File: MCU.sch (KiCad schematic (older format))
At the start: 9 parts

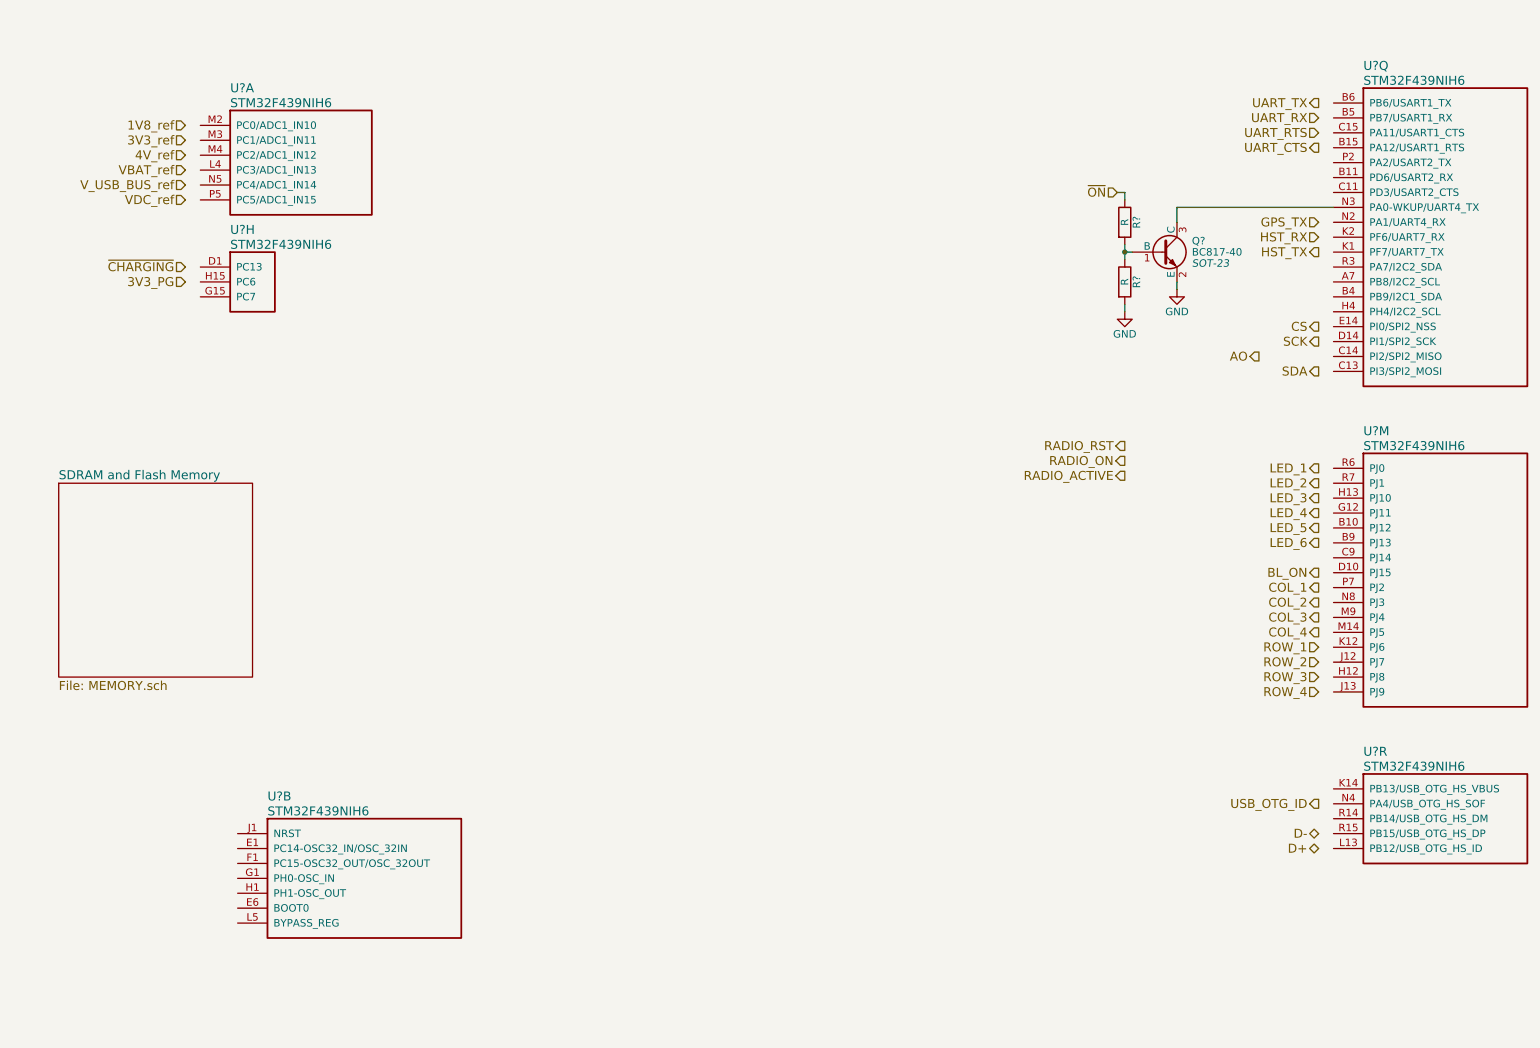
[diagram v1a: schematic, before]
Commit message: current version of the schematics. Audio circuits are still missing.
Audio curcuit topology
Audio from cellphone module is routed to STM
Audio from microphone is routed to STM
STM processes audio and routes microphone data to cellphone module
STM processes audio and routes cellphone audio to amplifier
analog multiplexer can switch route from mic directly to cellphone module and module to speaker
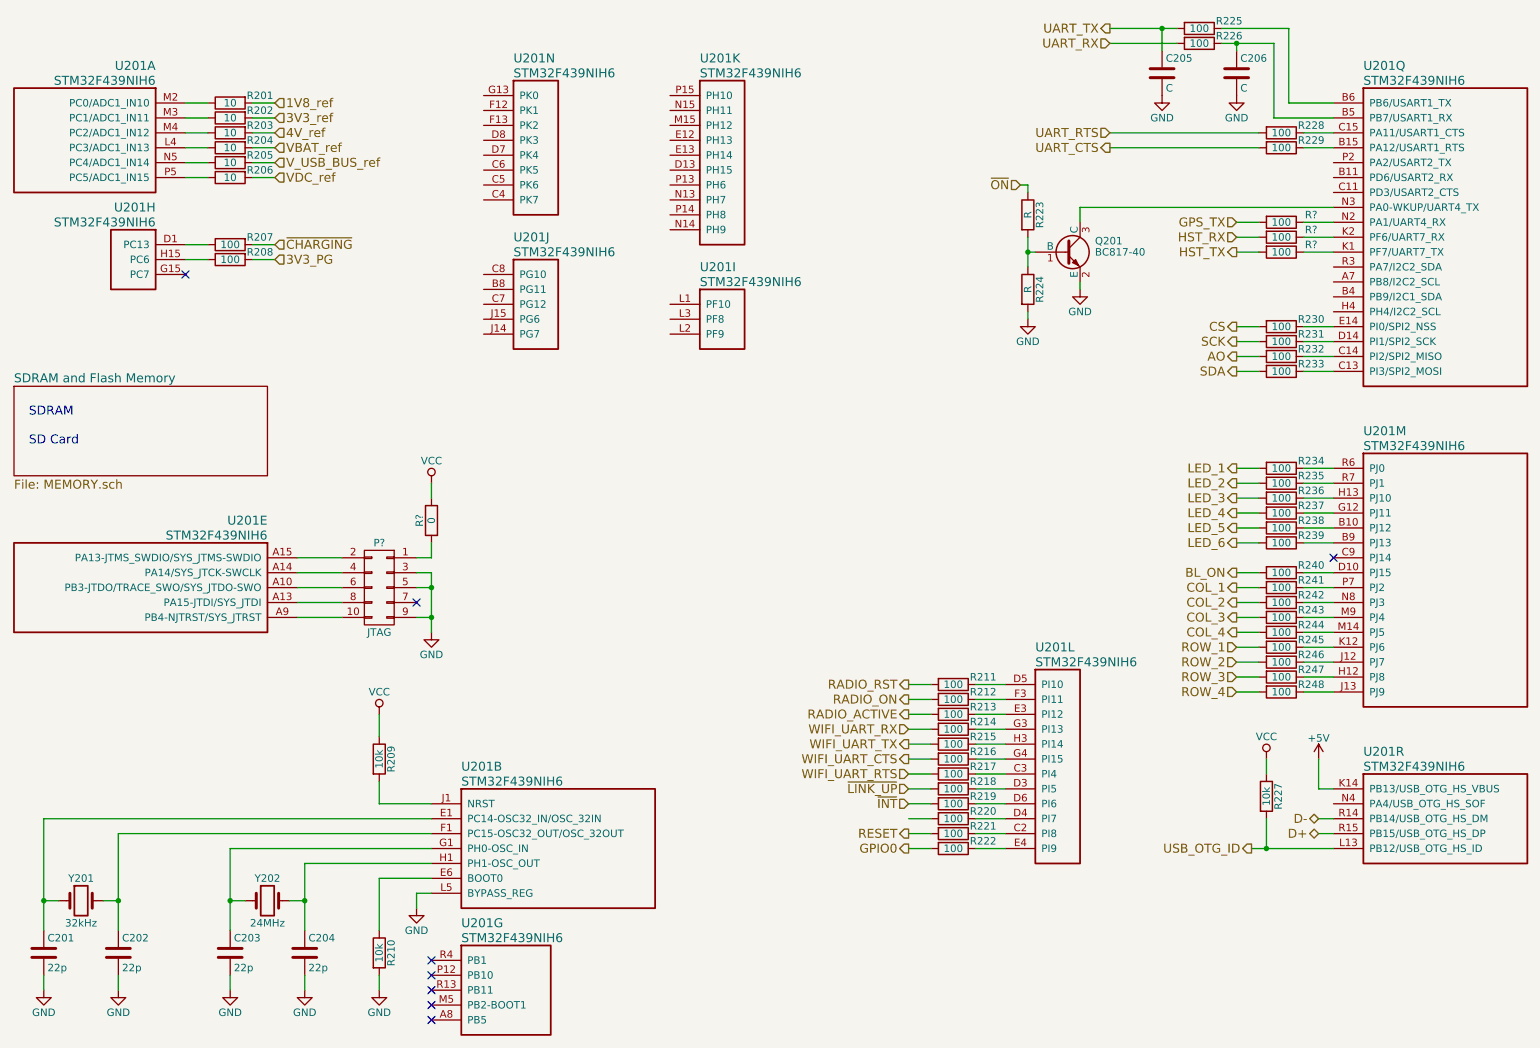
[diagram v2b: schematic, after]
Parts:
- added C201, C202, C203, C204: 22p, symbol C
- added C205, C206: C, symbol C
- added P?: JTAG, symbol CONN_02X05
- added R201, R202, R203, R204, R205, R206: 10, symbol R
- added R207, R208, R211, R212, R213, R214, R215, R216, R217, R218, R219, R220, R221, R222, R225, R226, R228, R229, R230, R231, R232, R233, R234, R235, R236, R237, R238, R239, R240, R241, R242, R243, R244, R245, R246, R247, R248, R? (x3): 100, symbol R
- added R209, R210, R227: 10k, symbol R
- added R?: 0, symbol R
- added unit 5 of U201
- added unit 11 of U201
- added unit 12 of U201
- added unit 14 of U201
- added unit 7 of U201
- added unit 9 of U201
- added unit 10 of U201
- added Y201: 32kHz, symbol Crystal
- added Y202: 24MHz, symbol Crystal
- Q201: renamed from Q?; footprint SOT-23 -> TO_SOT_Packages_SMD:SOT-23
- gave numbers to parts that had none: 3
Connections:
- net 1V8_ref: now also R201.2
- net 3V3_PG: now also R208.2
- net 3V3_ref: now also R202.2
- net 4V_ref: now also R203.2
- net AO: now also R232.2
- net BL_ON: now also R240.2
- net COL_1: now also R241.2
- net COL_2: now also R242.2
- net COL_3: now also R243.2
- net COL_4: now also R244.2
- net CS: now also R230.2
- net D+: now also U201.R15 (PB15/USB_OTG_HS_DP)
- net D-: now also U201.R14 (PB14/USB_OTG_HS_DM)
- net GND: now also U201.L5 (BYPASS_REG), C201.2, C202.2, C203.2, C204.2, C205.2, C206.2, P?.3 (P3), P?.5 (P5), P?.9 (P9), R210.2
- net GPS_TX: now also R?.2
- net HST_RX: now also R?.2
- net HST_TX: now also R?.2
- net LED_1: now also R234.2
- net LED_2: now also R235.2
- net LED_3: now also R236.2
- net LED_4: now also R237.2
- net LED_5: now also R238.2
- net LED_6: now also R239.2
- net RADIO_ACTIVE: now also R213.2
- net RADIO_ON: now also R212.2
- net RADIO_RST: now also R211.2
- net ROW_1: now also R245.2
- net ROW_2: now also R246.2
- net ROW_3: now also R247.2
- net ROW_4: now also R248.2
- net SCK: now also R231.2
- net SDA: now also R233.2
- net UART_CTS: now also R229.2
- net UART_RTS: now also R228.2
- net UART_RX: now also R226.2
- net UART_TX: now also C205.1, R225.2
- net USB_OTG_ID: now also U201.L13 (PB12/USB_OTG_HS_ID), R227.2
- net VBAT_ref: now also R204.2
- net VDC_ref: now also R206.2
- net V_USB_BUS_ref: now also R205.2
- net ~CHARGING: now also R207.2
- net at U201.L4 (PC3/ADC1_IN13): now also R204.1
- net at U201.M2 (PC0/ADC1_IN10): now also R201.1
- net at U201.M3 (PC1/ADC1_IN11): now also R202.1
- net at U201.M4 (PC2/ADC1_IN12): now also R203.1
- net at U201.N5 (PC4/ADC1_IN14): now also R205.1
- net at U201.P5 (PC5/ADC1_IN15): now also R206.1
- net at U201.D1 (PC13): now also R207.1
- net at U201.H15 (PC6): now also R208.1
- net at U201.B10 (PJ12): now also R238.1
- net at U201.B9 (PJ13): now also R239.1
- net at U201.D10 (PJ15): now also R240.1
- net at U201.G12 (PJ11): now also R237.1
- net at U201.H12 (PJ8): now also R247.1
- net at U201.H13 (PJ10): now also R236.1
- net at U201.J12 (PJ7): now also R246.1
- net at U201.J13 (PJ9): now also R248.1
- net at U201.K12 (PJ6): now also R245.1
- net at U201.M14 (PJ5): now also R244.1
- net at U201.M9 (PJ4): now also R243.1
- net at U201.N8 (PJ3): now also R242.1
- net at U201.P7 (PJ2): now also R241.1
- net at U201.R6 (PJ0): now also R234.1
- net at U201.R7 (PJ1): now also R235.1
- net at U201.E1 (PC14-OSC32_IN/OSC_32IN): now also C201.1, Y201.1
- net at U201.E6 (BOOT0): now also R210.1
- net at U201.F1 (PC15-OSC32_OUT/OSC_32OUT): now also C202.1, Y201.2
- net at U201.G1 (PH0-OSC_IN): now also C203.1, Y202.1
- net at U201.H1 (PH1-OSC_OUT): now also C204.1, Y202.2
- net at U201.J1 (NRST): now also R209.2
- net at U201.B15 (PA12/USART1_RTS): now also R229.1
- net at U201.B5 (PB7/USART1_RX): now also C206.1, R226.1
- net at U201.B6 (PB6/USART1_TX): now also R225.1
- net at U201.C13 (PI3/SPI2_MOSI): now also R233.1
- net at U201.C14 (PI2/SPI2_MISO): now also R232.1
- net at U201.C15 (PA11/USART1_CTS): now also R228.1
- net at U201.D14 (PI1/SPI2_SCK): now also R231.1
- net at U201.E14 (PI0/SPI2_NSS): now also R230.1
- net at U201.K1 (PF7/UART7_TX): now also R?.1
- net at U201.K2 (PF6/UART7_RX): now also R?.1
- net at U201.N2 (PA1/UART4_RX): now also R?.1
- net +5V: now reaches U201.K14 (PB13/USB_OTG_HS_VBUS)
- new net: P?.6 (P6), U201.A10 (PB3-JTDO/TRACE_SWO/SYS_JTDO-SWO)
- new net: P?.8 (P8), U201.A13 (PA15-JTDI/SYS_JTDI)
- new net: P?.4 (P4), U201.A14 (PA14/SYS_JTCK-SWCLK)
- new net: P?.2 (P2), U201.A15 (PA13-JTMS_SWDIO/SYS_JTMS-SWDIO)
- new net: P?.10 (P10), U201.A9 (PB4-NJTRST/SYS_JTRST)
- new net: R221.1, U201.C2 (PI8)
- new net: R217.1, U201.C3 (PI4)
- new net: R218.1, U201.D3 (PI5)
- new net: R220.1, U201.D4 (PI7)
- new net: R211.1, U201.D5 (PI10)
- new net: R219.1, U201.D6 (PI6)
- new net: R213.1, U201.E3 (PI12)
- new net: R222.1, U201.E4 (PI9)
- new net: R212.1, U201.F3 (PI11)
- new net: R214.1, U201.G3 (PI13)
- new net: R216.1, U201.G4 (PI15)
- new net: R215.1, U201.H3 (PI14)
- new net: P?.1 (P1), R?.2
- new net GPIO0: R222.2
- new net RESET: R221.2
- new net VCC: R209.1, R227.1, R?.1
- new net WIFI_UART_CTS: R216.2
- new net WIFI_UART_RTS: R217.2
- new net WIFI_UART_RX: R214.2
- new net WIFI_UART_TX: R215.2
- new net ~INT: R219.2
- new net ~LINK_UP: R218.2
- no-connect marks 0 -> 8
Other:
- note added: "SDRAM\n\nSD Card"
- moved on the sheet: Q201, R223, R224, U201A, U201B, U201H

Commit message: added Ti WL1807/1837 Module for WLAN and Bluetooth. added Test Points
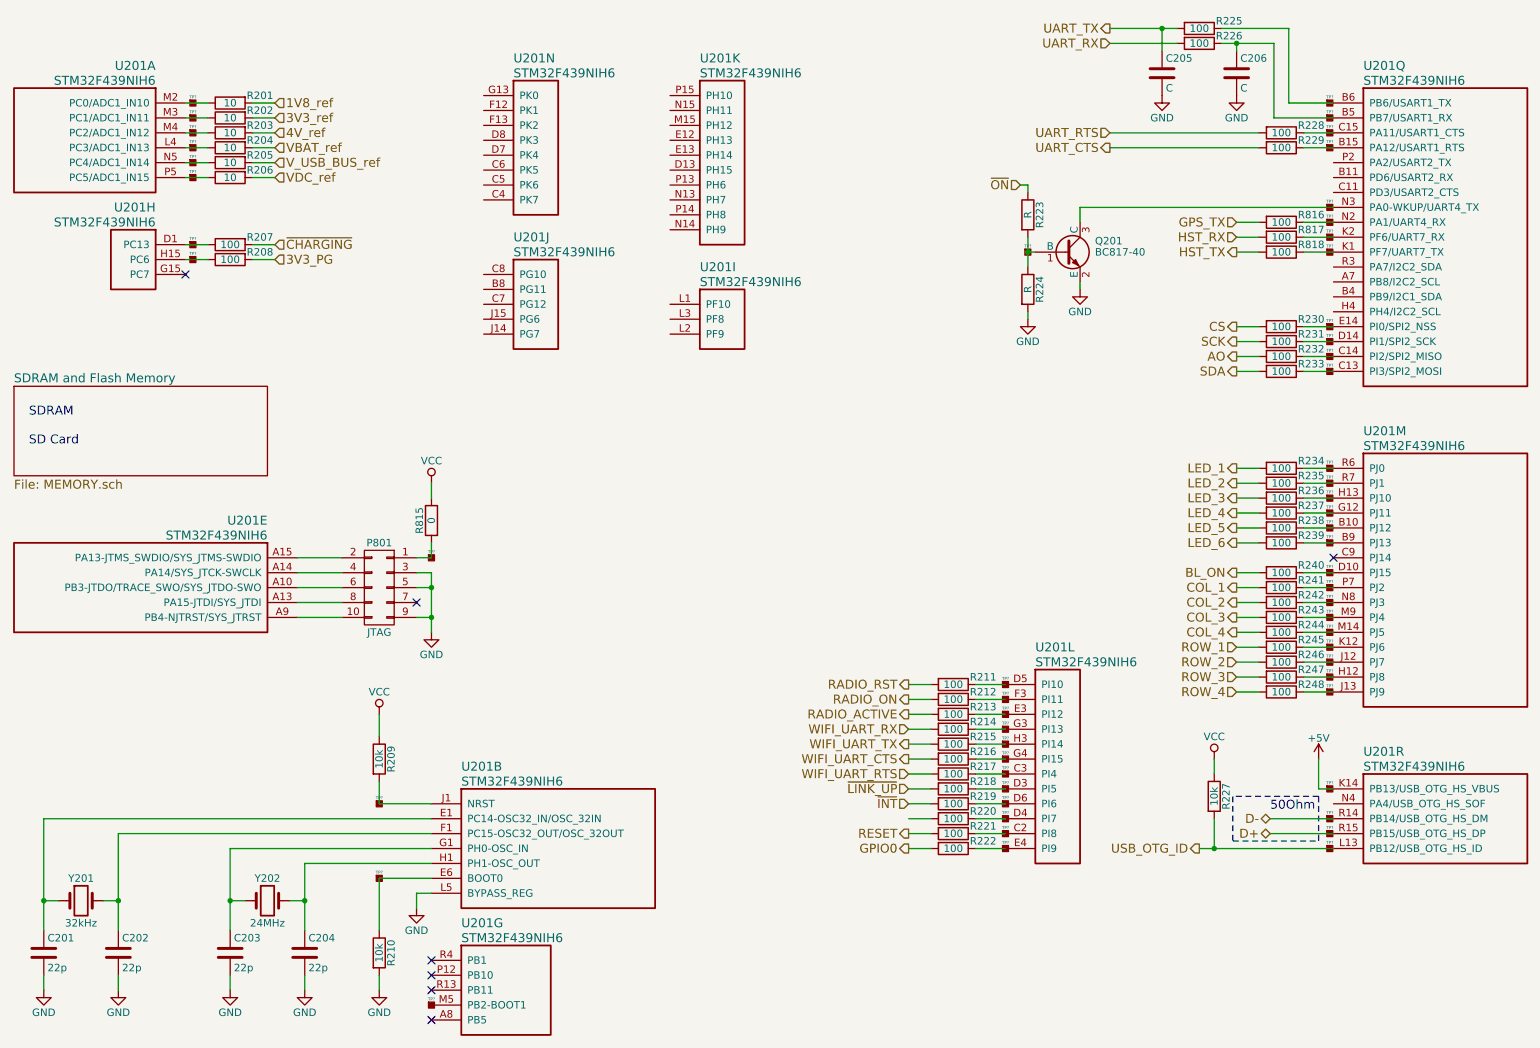
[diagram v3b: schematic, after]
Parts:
- added TP? (x56): TP, symbol TP
- gave numbers to parts that had none: 5
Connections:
- net at R210.1, U201.E6 (BOOT0): now also TP?.1
- net at R209.2, U201.J1 (NRST): now also TP?.1
- net at Q201.1 (B), R223.2, R224.1: now also TP?.1
- net at R221.1, U201.C2 (PI8): now also TP?.1
- net at R217.1, U201.C3 (PI4): now also TP?.1
- net at R218.1, U201.D3 (PI5): now also TP?.1
- net at R220.1, U201.D4 (PI7): now also TP?.1
- net at R211.1, U201.D5 (PI10): now also TP?.1
- net at R219.1, U201.D6 (PI6): now also TP?.1
- net at R213.1, U201.E3 (PI12): now also TP?.1
- net at R222.1, U201.E4 (PI9): now also TP?.1
- net at R212.1, U201.F3 (PI11): now also TP?.1
- net at R214.1, U201.G3 (PI13): now also TP?.1
- net at R216.1, U201.G4 (PI15): now also TP?.1
- net at R215.1, U201.H3 (PI14): now also TP?.1
- net at U201.M5 (PB2-BOOT1): now also TP?.1
- net at P801.1 (P1), R815.2: now also TP?.1
- no-connect marks 8 -> 7
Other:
- note added: "50Ohm"
- moved on the sheet: R227

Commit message: moved to some Bus routing for serveral communication signals on the top sheet. This reduces lines on the top sheet.
Changed 4V boost converter circuit toi use TPS61046 for size reasons
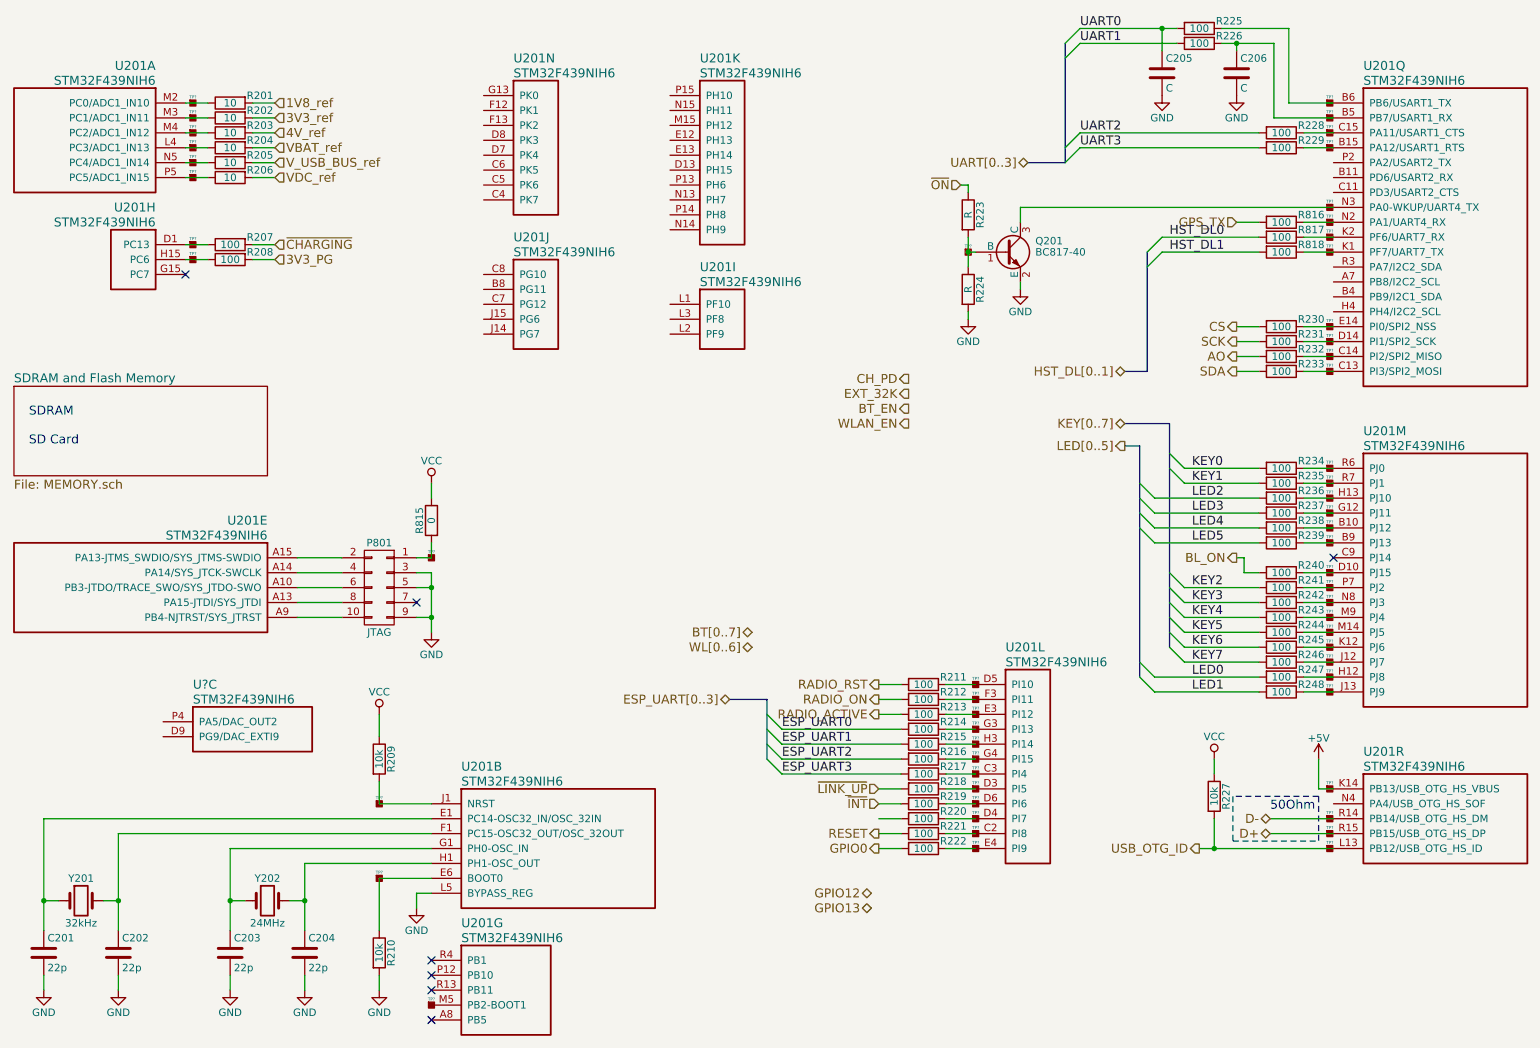
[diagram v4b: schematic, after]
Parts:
- added U?: STM32F439NIH6, symbol STM32F439NIH6
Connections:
- net COL_1 renamed KEY2
- net COL_2 renamed KEY3
- net COL_3 renamed KEY4
- net COL_4 renamed KEY5
- net HST_RX renamed HST_DL0
- net HST_TX renamed HST_DL1
- net LED_1 renamed KEY0
- net LED_2 renamed KEY1
- net LED_3 renamed LED2
- net LED_4 renamed LED3
- net LED_5 renamed LED4
- net LED_6 renamed LED5
- net ROW_1 renamed KEY6
- net ROW_2 renamed KEY7
- net ROW_3 renamed LED0
- net ROW_4 renamed LED1
- net UART_CTS renamed UART3
- net UART_RTS renamed UART2
- net UART_RX renamed UART1
- net UART_TX renamed UART0
- net WIFI_UART_CTS renamed ESP_UART2
- net WIFI_UART_RTS renamed ESP_UART3
- net WIFI_UART_RX renamed ESP_UART0
- net WIFI_UART_TX renamed ESP_UART1
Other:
- moved on the sheet: Q201, R211, R212, R213, R214, R215, R216, R217, R218, R219, R220, R221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

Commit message: aktuelle Version
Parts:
- C201, C202, C203, C204, C205, C206: footprint (none) -> Capacitors_SMD:C_0603
- P801: footprint (none) -> Pin_Headers:Pin_Header_Straight_2x05_Pitch1.27mm
- R201, R202, R203, R204, R205, R206, R207, R208, R209, R210, R211, R212, R213, R214, R215, R216, R217, R218, R219, R220, R221, R222, R223, R224, R225, R226, R227, R228, R229, R230, R231, R232, R233, R234, R235, R236, R237, R238, R239, R240, R241, R242, R243, R244, R245, R246, R247, R248, R815, R816, R817, R818: footprint (none) -> Resistors_SMD:R_0603
- TP801, TP802, TP803, TP804, TP805, TP806, TP807, TP808, TP809, TP810, TP811, TP812, TP813, TP814, TP815, TP816, TP817, TP818, TP819, TP820, TP821, TP822, TP823, TP824, TP825, TP826, TP827, TP828, TP829, TP830, TP831, TP832, TP833, TP834, TP835, TP836, TP837, TP838, TP839, TP840, TP841, TP842, TP843, TP844, TP845, TP846, TP847, TP848, TP849, TP850, TP851, TP852, TP853, TP854, TP855, TP856: renamed from TP?; footprint (none) -> buttons:TP
- gave numbers to parts that had none: 1
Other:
- note added: "9"
